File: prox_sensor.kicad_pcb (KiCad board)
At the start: 4 copper layers, 25.1 x 45.3 mm, 37 parts, among them J1 +, J12 Conn_01x05, J2 -, J3 A, J9 K, U1 BD4840G-TR, U2 STM32L031G6U6, U3 STHS34PF80, U4 VL53L0CXV0DH1, U5 TPS61165DBV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

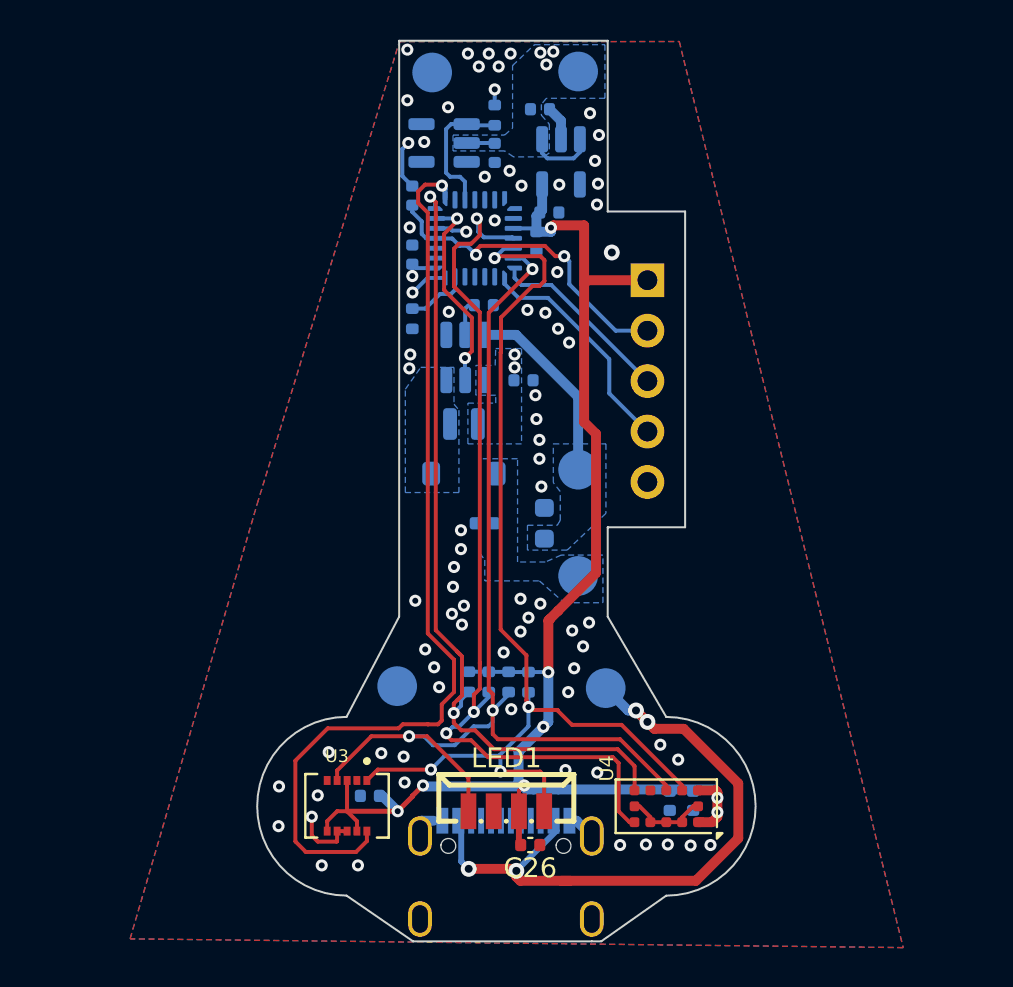
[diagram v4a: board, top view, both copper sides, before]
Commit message: Hole for VEML7700
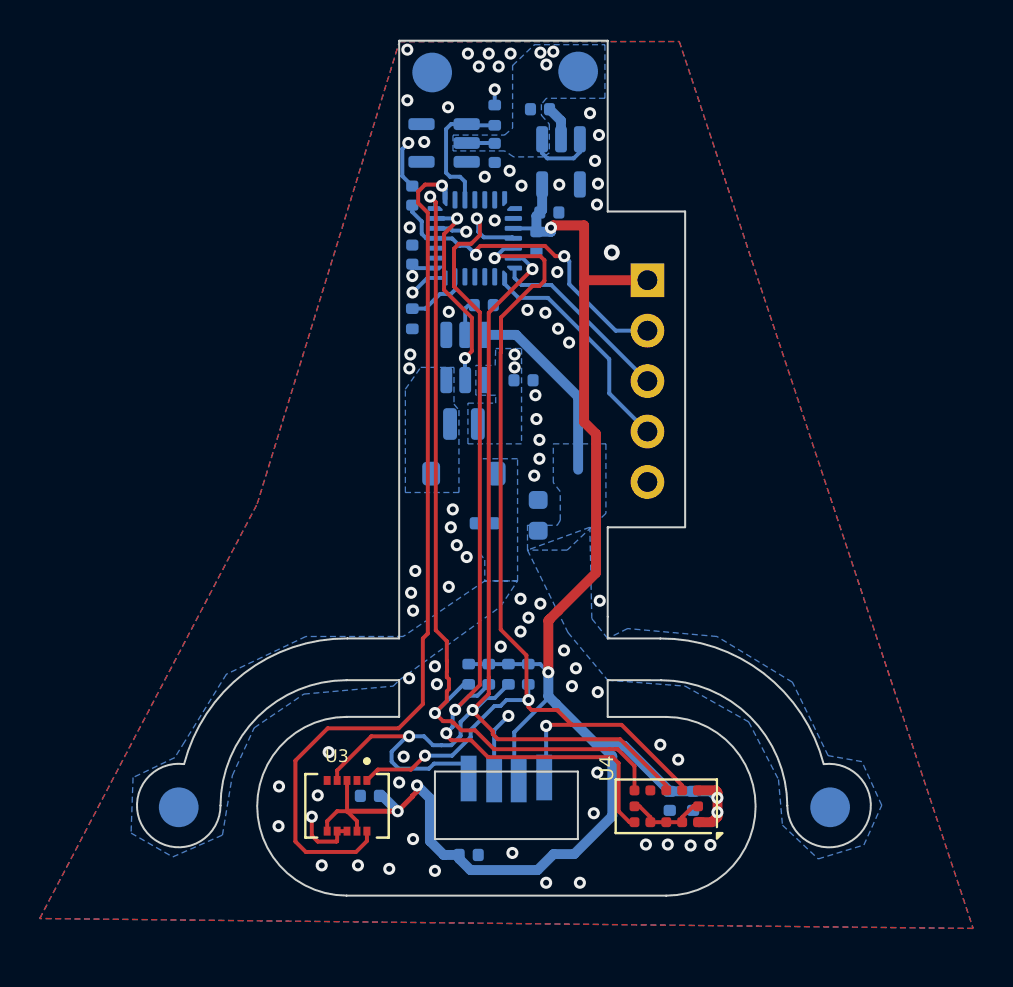
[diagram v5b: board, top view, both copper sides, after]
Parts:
- removed GND1, VBUS1: -, TestPoint:TestPoint_Pad_D2.0mm
- removed USBC1: ~, 1-COB-MOD:USB-C_SMD-TYPE-C-31-M-12
- C26, LED1: moved to B.Cu
- moved J3 23.2 mm to (129.2, 167.1)
- moved J9 21.2 mm to (162.0, 167.1)
- moved C26 3.14 mm to (143.8, 169.5)
- moved LED1 1.30 mm to (145.7, 166.0)
- moved R7 0.51 mm to (147.3, 152.4)
- moved R18 0.40 mm to (146.8, 160.4)
- moved R20 0.39 mm to (145.8, 160.4)
- moved R2 0.39 mm to (144.8, 160.4)
- moved R3 0.38 mm to (143.8, 160.4)
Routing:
- net Net-(VBUS1-Pin_1): track 33.2 -> 0.00 mm, vias 4 -> 0
- net +3V3: track 83.1 -> 92.3 mm, vias 11 -> 9
- net /Mcu-unit: STM32/PA2_STH_GPIO_INT: track 46.6 -> 44.4 mm
- net /Mcu-unit: STM32/PA10_I2C_SDA: track 52.8 -> 54.5 mm
- net /Mcu-unit: STM32/PA1_ToF_GPIO: track 40.6 -> 42.1 mm
- net /Mcu-unit: STM32/PA9_I2C_SCL: track 53.5 -> 52.1 mm
- net GND: track 16.6 -> 17.4 mm, vias 77 -> 81
- net /Mcu-unit: STM32/PA8_ToF_XSHUT: track 45.0 -> 45.8 mm
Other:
- board size 25.1 x 45.3 mm -> 37 x 43 mm

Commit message: Refactoring
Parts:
- added ?: , , F.Cu at (146.3, 170.1)
- added J10: K, Connector_PinHeader_1.27mm:PinHeader_1x01_P1.27mm_Vertical, B.Cu at (128.8, 165.8)
- added J4: A, Connector_PinHeader_1.27mm:PinHeader_1x01_P1.27mm_Vertical, B.Cu at (161.2, 167.9)
- added REF**: TestPoint_Pad_D2.0mm, TestPoint:TestPoint_Pad_D2.0mm, B.Cu at (145.1, 170.1)
- J3, J9: footprint TestPoint:TestPoint_Pad_D2.0mm -> Connector_PinHeader_1.27mm:PinHeader_1x01_P1.27mm_Vertical
- moved R2 8.09 mm to (151.6, 164.8)
- moved R3 8.02 mm to (150.5, 164.8)
- moved C26 6.17 mm to (145.6, 163.6), turned to 0 degrees
- moved J9 1.22 mm to (162.2, 165.9), turned to 180 degrees
- moved J3 1.12 mm to (129.7, 168.1), turned to 180 degrees
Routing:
- net /Mcu-unit: STM32/PA1_ToF_GPIO: track 42.1 -> 57.8 mm, vias 2 -> 3
- net +3V3: track 92.3 -> 83.2 mm, vias 9 -> 10
- net /Mcu-unit: STM32/PA10_I2C_SDA: track 54.5 -> 51.5 mm
- net /Mcu-unit: STM32/PA9_I2C_SCL: track 52.1 -> 53.8 mm
- net /Mcu-unit: STM32/PA8_ToF_XSHUT: track 45.8 -> 44.8 mm, vias 3 -> 2
- net GND: vias 81 -> 100
- net /TPS61165/LEDK: vias 0 -> 8
- added copper zone on In2.Cu, net /TPS61165/LEDK
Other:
- outline, holes or cut-outs redrawn

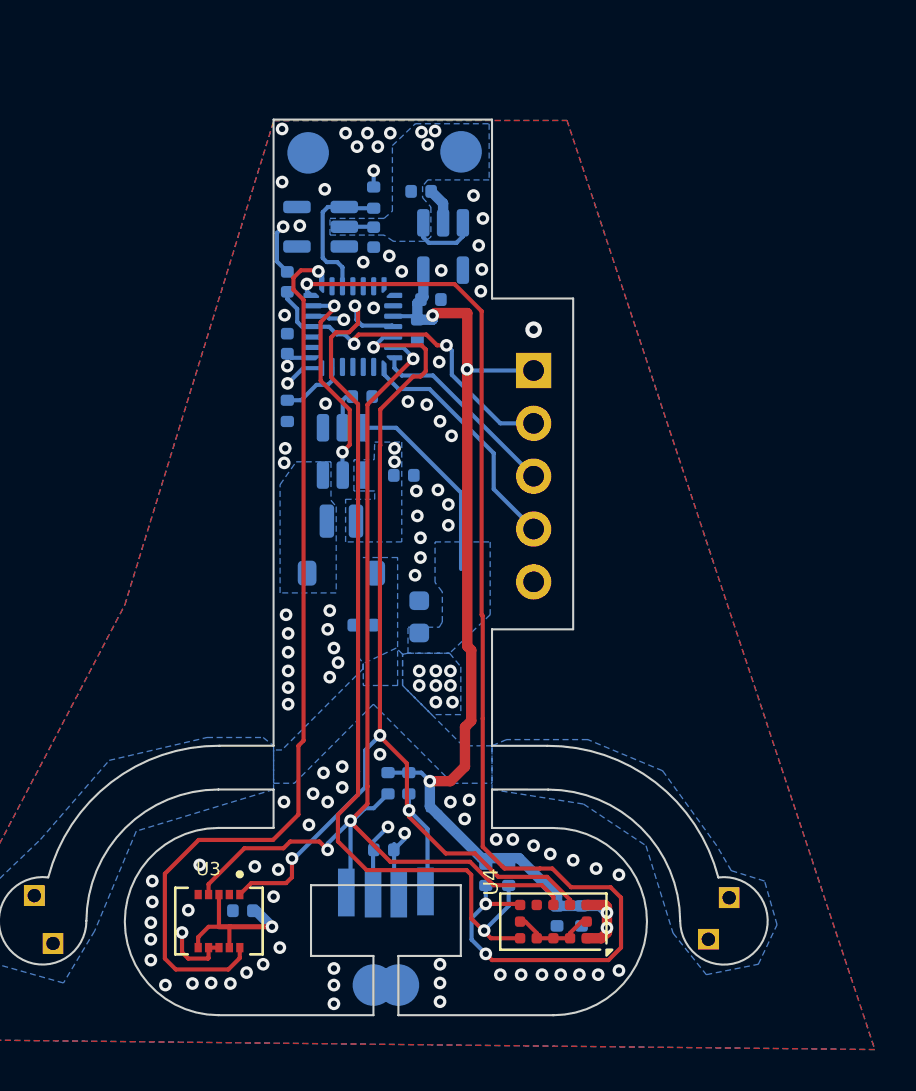
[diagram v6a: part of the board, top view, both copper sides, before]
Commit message: Adding power control and extra input, to attach another som
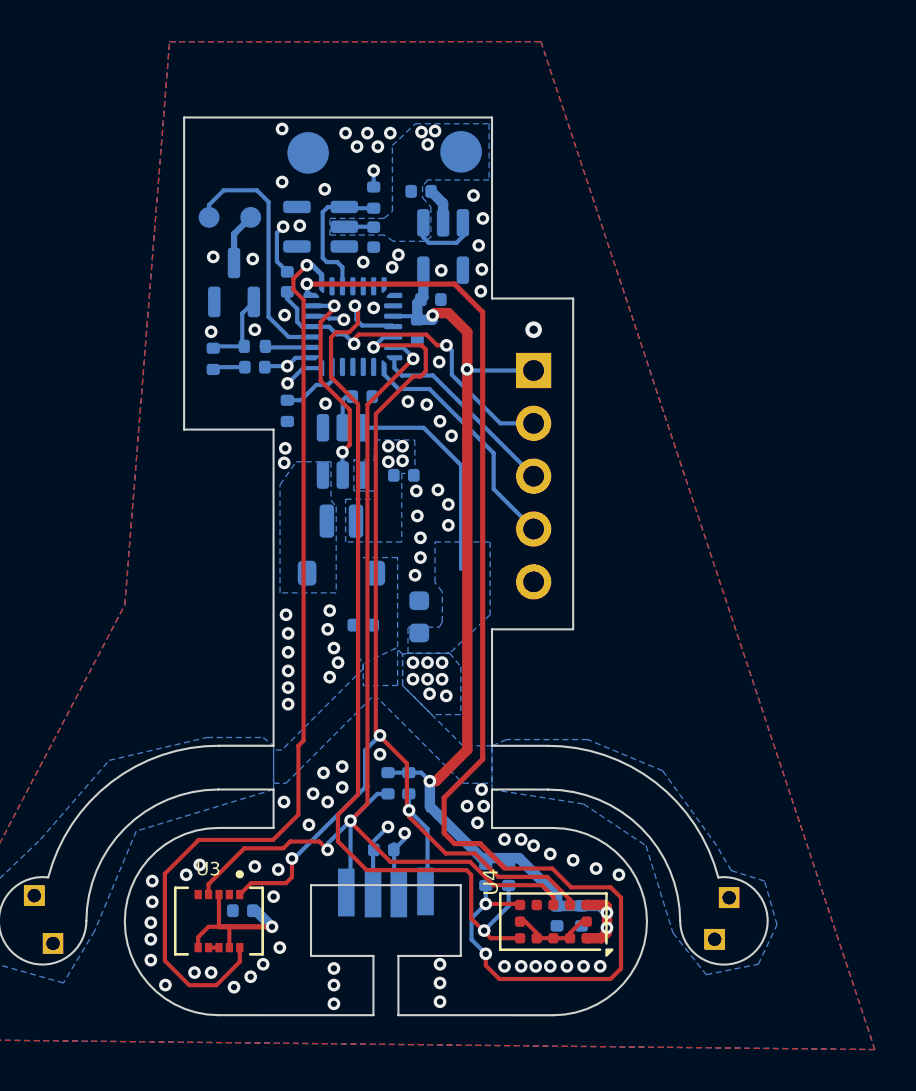
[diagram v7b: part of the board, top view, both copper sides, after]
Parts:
- removed ?: , 
- removed REF**: TestPoint_Pad_D2.0mm, TestPoint:TestPoint_Pad_D2.0mm
- added J5: -, TestPoint:TestPoint_Pad_D1.0mm, B.Cu at (139.2, 133.2)
- added J7: sw, TestPoint:TestPoint_Pad_D1.0mm, B.Cu at (137.2, 133.2)
- added Q1: AO3400A, Package_TO_SOT_SMD:SOT-23, B.Cu at (138.4, 136.4)
- added R5: 100k, Resistor_SMD:R_0402_1005Metric, B.Cu at (137.4, 140.0)
- added R6: 100Ohm, Resistor_SMD:R_0402_1005Metric, B.Cu at (139.4, 139.4)
- moved C7 1.93 mm to (139.4, 140.4), turned to 180 degrees
- moved J4 0.30 mm to (161.5, 167.9)
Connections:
- U2 pad 2: unconnected-(U2-PC14-Pad2) -> /Mcu-unit: STM32/PC_14
- U2 pad 3: unconnected-(U2-PC15-Pad3) -> /Mcu-unit: STM32/PC_15
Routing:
- net /Mcu-unit: STM32/PC_15: track 0.00 -> 12.0 mm
- net /Mcu-unit: STM32/PA1_ToF_GPIO: track 57.8 -> 61.7 mm
- net Net-(Q1-G): track 0.00 -> 3.80 mm
- net Net-(J5-Pin_1): track 0.00 -> 2.52 mm
- net /Mcu-unit: STM32/PC_14: track 0.00 -> 2.48 mm
- net GND: track 17.4 -> 16.1 mm, vias 100 -> 104
- net /Mcu-unit: STM32/PA2_STH_GPIO_INT: track 44.4 -> 45.4 mm
- net /TPS61165/LEDK: track 9.72 -> 10.5 mm
- net +3V3: track 83.2 -> 82.7 mm
- net +BATT: vias 5 -> 7
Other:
- board size 37 x 43 mm -> 37 x 43.1 mm
- board text added: "PWR"
- board text added: "SW"
